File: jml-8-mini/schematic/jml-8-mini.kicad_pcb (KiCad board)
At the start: 4 copper layers, 99.9 x 99.9 mm, 48 parts, among them J1 BarrelJack, J2 SIO CHB, J3 UART, J5 Address Decoding, J6 Z80 Lines, SW1 Reset, SW2 Power, U1 Z80CPU, U10 74LS74, U11 NE555P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

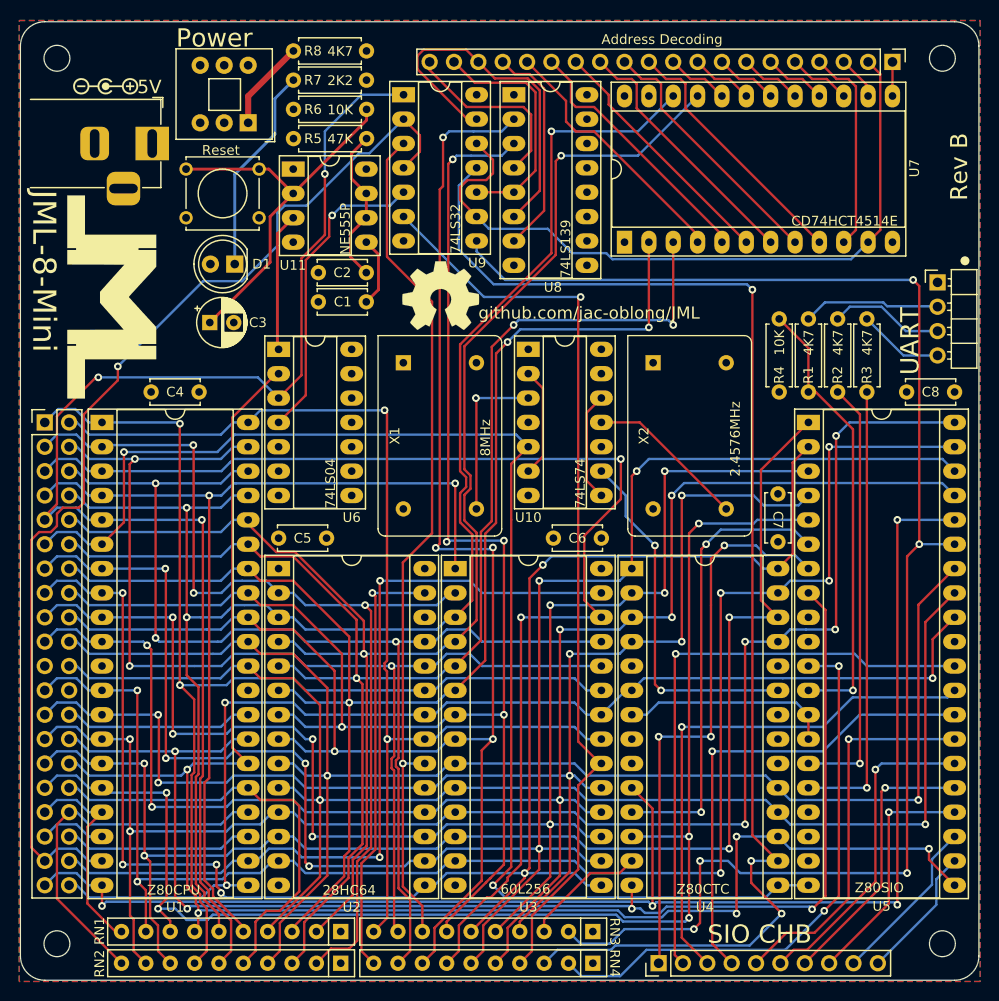
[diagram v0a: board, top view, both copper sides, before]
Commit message: change layers 2 & 3 to GND and put PWR on top and bottom, regenerate gerbers
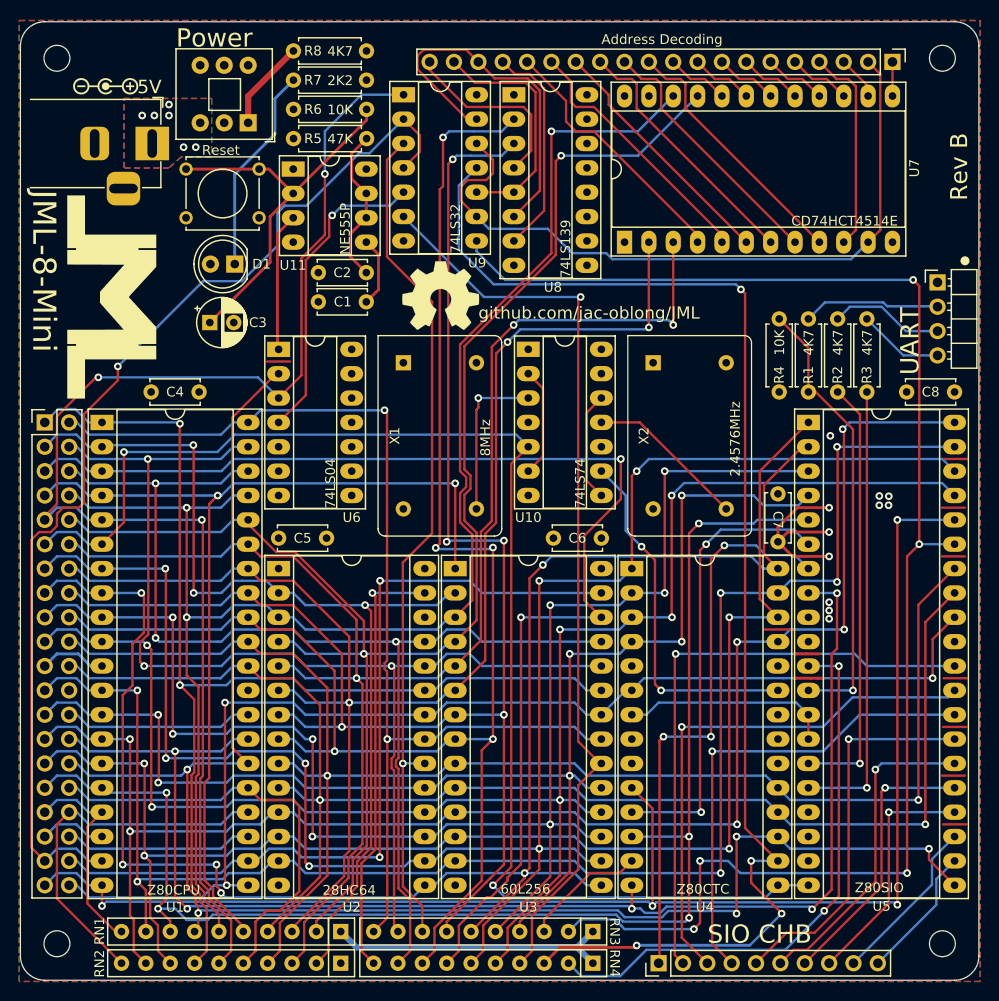
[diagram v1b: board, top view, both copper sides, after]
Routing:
- net +5V: track 0.00 -> 84.2 mm, vias 0 -> 11
- net /D3: track 172.8 -> 177.4 mm
- net /~{M1}: track 139.4 -> 142.1 mm, vias 4 -> 5
- net /A9: track 121.4 -> 120.2 mm
- net /A12: track 102.5 -> 101.4 mm
- net /~{CTC}: track 138.8 -> 138.1 mm, vias 3 -> 4
- net /D0: track 162.7 -> 163.3 mm
- net /Power, Clock and Reset/PWR_IN: vias 0 -> 6
- added copper zone on B.Cu, net +5V
- added copper zone on F.Cu, net +5V
- added copper zone on B.Cu, net /Power, Clock and Reset/PWR_IN
- added copper zone on F.Cu, net /Power, Clock and Reset/PWR_IN
- added copper zone on In2.Cu, net GND
- removed copper zone on In2.Cu, net +5V
- removed copper zone on In2.Cu, net /Power, Clock and Reset/PWR_IN
- removed copper zone on B.Cu, net GND
- removed copper zone on F.Cu, net GND

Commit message: fix two capacitor footprints being swapped
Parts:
- C2: footprint Capacitor_THT:C_Disc_D5.0mm_W2.5mm_P5.00mm -> Capacitor_THT:CP_Radial_D5.0mm_P2.50mm
- C3: footprint Capacitor_THT:CP_Radial_D5.0mm_P2.50mm -> Capacitor_THT:C_Disc_D5.0mm_W2.5mm_P5.00mm
- moved C2 14.9 mm to (117.5, 72.6)
- moved C3 12.5 mm to (126.3, 67.2)
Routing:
- net /Power, Clock and Reset/555Dis/Thr: track 16.6 -> 33.1 mm, vias 0 -> 1
- net /Power, Clock and Reset/555Trigger: track 41.2 -> 33.5 mm
- net /~{MREQ}: track 113.6 -> 115.0 mm

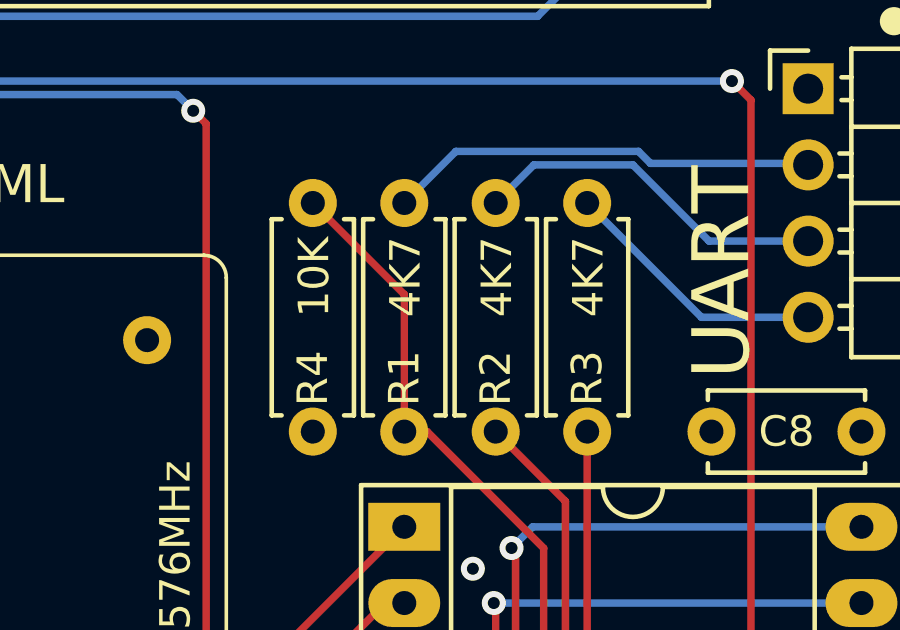
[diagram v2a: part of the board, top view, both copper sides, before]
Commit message: fix incorrect value for resistor
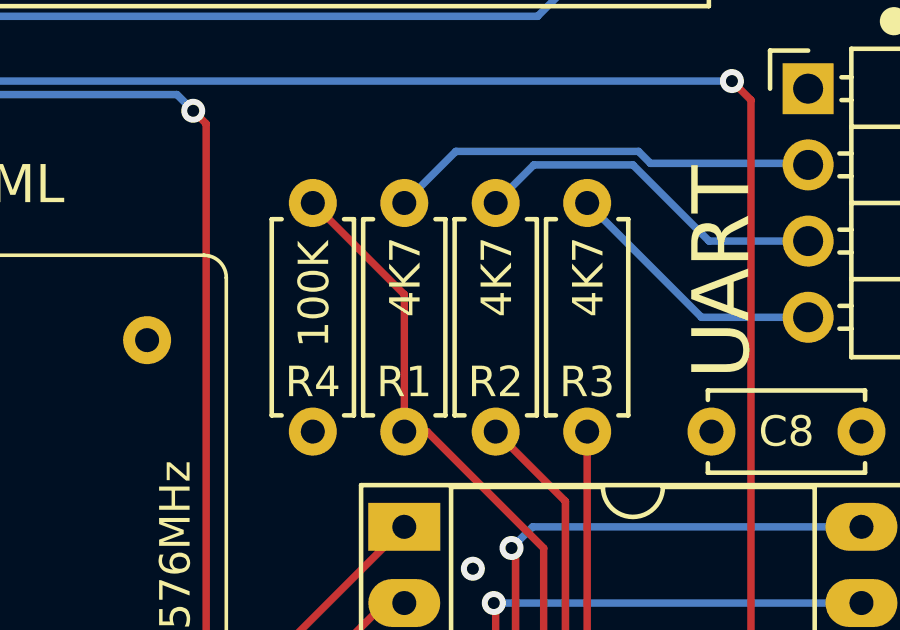
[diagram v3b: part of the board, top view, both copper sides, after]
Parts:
- R4: value 10K -> 100K
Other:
- board text added: "100K"
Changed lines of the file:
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@@
     (property "ki_keywords" "R resistor")
     (attr through_hole)
-    (fp_text reference "R1" (at 5.842 0 -270 unlocked) (layer "F.SilkS")
+    (fp_text reference "R1" (at 5.969 0 unlocked) (layer "F.SilkS")
         (effects (font (size 1.016 1.016) (thickness 0.1524)))
     )
@@
     (property "ki_keywords" "R resistor")
     (attr through_hole)
-    (fp_text reference "R4" (at 1.778 0 90 unlocked) (layer "F.SilkS")
+    (fp_text reference "R4" (at 1.651 0 unlocked) (layer "F.SilkS")
         (effects (font (size 1.016 1.016) (thickness 0.1524)))
     )
-    (fp_text value "10K" (at 5.334 0 90 unlocked) (layer "F.Fab")
+    (fp_text value "100K" (at 4.826 0 90 unlocked) (layer "F.Fab")
         (effects (font (size 1 1) (thickness 0.15)))
     )
@@
     (property "ki_keywords" "R resistor")
     (attr through_hole)
-    (fp_text reference "R2" (at 5.842 0 -270 unlocked) (layer "F.SilkS")
+    (fp_text reference "R2" (at 5.969 0 unlocked) (layer "F.SilkS")
         (effects (font (size 1.016 1.016) (thickness 0.1524)))
     )
@@
     (property "ki_keywords" "R resistor")
     (attr through_hole)
-    (fp_text reference "R3" (at 5.842 0 -270 unlocked) (layer "F.SilkS")
+    (fp_text reference "R3" (at 5.969 0 unlocked) (layer "F.SilkS")
         (effects (font (size 1.016 1.016) (thickness 0.1524)))
     )
@@
     (effects (font (size 1.016 1.016) (thickness 0.1524)) (justify left bottom))
   )
-  (gr_text "10K" (at 175.006 75.819 90) (layer "F.SilkS")
+  (gr_text "100K" (at 175.006 76.835 90) (layer "F.SilkS")
     (effects (font (size 1.016 1.016) (thickness 0.1524)) (justify left bottom))
   )
